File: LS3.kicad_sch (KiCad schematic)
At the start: 6 parts, among them Q5 VND14NV04-E, Q6 VND14NV04-E, Q7 VND14NV04-E

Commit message: Vendor DPAK/R0603 footprints for Update PCB without submodule gaps
Frame inj/LS sheets now use microcore-fp (in-repo footprints/) so KiCad
finds DPAK and R0603 even when hellen-one-common is missing from a zip
checkout. Keep hellen-one-common for Mini-B and other shared parts.
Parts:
- Q5, Q6, Q7: footprint hellen-one-common:DPAK -> microcore-fp:DPAK
- R5, R6, R7: footprint hellen-one-common:R0603 -> microcore-fp:R0603
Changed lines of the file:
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@@
 			)
 		)
-		(property "Footprint" "hellen-one-common:DPAK"
+		(property "Footprint" "microcore-fp:DPAK"
 			(at 101.6 25.4 0)
 			(effects
@@
 			)
 		)
-		(property "Footprint" "hellen-one-common:R0603"
+		(property "Footprint" "microcore-fp:R0603"
 			(at 139.7 25.4 0)
 			(effects
@@
 			)
 		)
-		(property "Footprint" "hellen-one-common:DPAK"
+		(property "Footprint" "microcore-fp:DPAK"
 			(at 101.6 55.879999999999995 0)
 			(effects
@@
 			)
 		)
-		(property "Footprint" "hellen-one-common:R0603"
+		(property "Footprint" "microcore-fp:R0603"
 			(at 139.7 55.879999999999995 0)
 			(effects
@@
 			)
 		)
-		(property "Footprint" "hellen-one-common:DPAK"
+		(property "Footprint" "microcore-fp:DPAK"
 			(at 101.6 86.36 0)
 			(effects
@@
 			)
 		)
-		(property "Footprint" "hellen-one-common:R0603"
+		(property "Footprint" "microcore-fp:R0603"
 			(at 139.7 86.36 0)
 			(effects

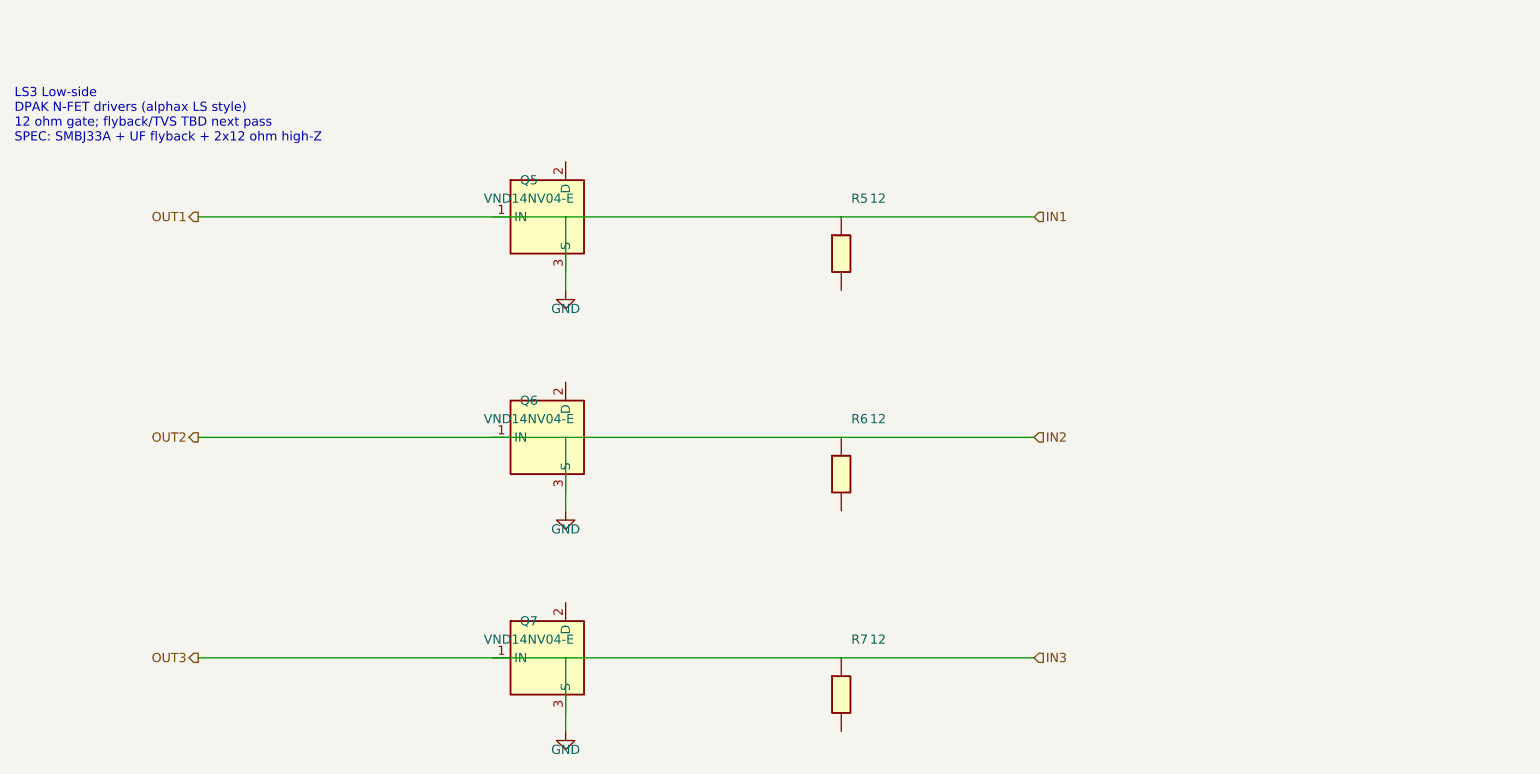
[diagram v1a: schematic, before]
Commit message: Fix top schematic wiring so labels connect to Hellen module pins
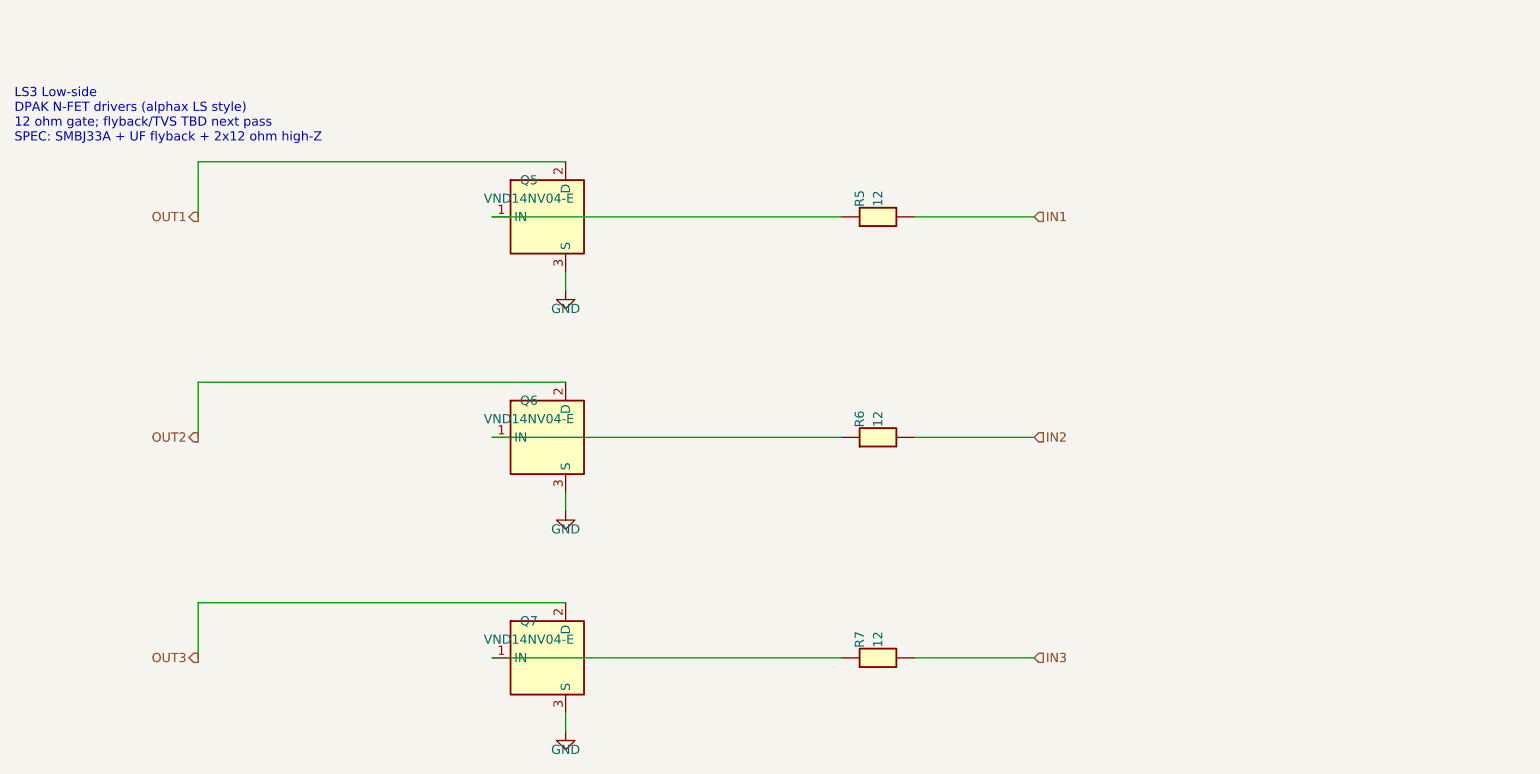
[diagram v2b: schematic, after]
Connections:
- net GND: now also Q5.3 (S), Q6.3 (S), Q7.3 (S); no longer R5.1, R6.1, R7.1
- net IN3: now reaches R7.2
- net at Q6.1 (IN): now also R6.1
- net OUT2: now reaches Q6.2 (D)
- net IN2: now reaches R6.2
- net at Q5.1 (IN): now also R5.1
- net OUT1: now reaches Q5.2 (D)
- net at Q7.1 (IN): now also R7.1
- net OUT3: now reaches Q7.2 (D)
- net IN1: now reaches R5.2
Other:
- moved on the sheet: R5, R6, R7
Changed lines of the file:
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@@
 	(symbol
 		(lib_id "hellen-one-common:Res")
-		(at 139.7 25.4 270)
+		(at 139.7 25.4 0)
 		(unit 1)
 		(exclude_from_sim no)
@@
 	(symbol
 		(lib_id "hellen-one-common:Res")
-		(at 139.7 55.879999999999995 270)
+		(at 139.7 55.879999999999995 0)
 		(unit 1)
 		(exclude_from_sim no)
@@
 	(symbol
 		(lib_id "hellen-one-common:Res")
-		(at 139.7 86.36 270)
+		(at 139.7 86.36 0)
 		(unit 1)
 		(exclude_from_sim no)
@@
 		)
 	)
-	(wire
-		(pts
-			(xy 50.8 25.4) (xy 101.6 25.4)
-		)
-		(stroke
-			(width 0)
-			(type default)
-		)
-	)
-	(wire
-		(pts
-			(xy 101.6 25.4) (xy 139.7 25.4)
-		)
-		(stroke
-			(width 0)
-			(type default)
-		)
-	)
-	(wire
-		(pts
-			(xy 139.7 25.4) (xy 166.37 25.4)
-		)
-		(stroke
-			(width 0)
-			(type default)
-		)
-	)
-	(wire
-		(pts
-			(xy 101.6 25.4) (xy 101.6 35.56)
-		)
-		(stroke
-			(width 0)
-			(type default)
-		)
-	)
-	(wire
-		(pts
-			(xy 50.8 55.879999999999995) (xy 101.6 55.879999999999995)
-		)
-		(stroke
-			(width 0)
-			(type default)
-		)
-	)
-	(wire
-		(pts
-			(xy 101.6 55.879999999999995) (xy 139.7 55.879999999999995)
-		)
-		(stroke
-			(width 0)
-			(type default)
-		)
-	)
-	(wire
-		(pts
-			(xy 139.7 55.879999999999995) (xy 166.37 55.879999999999995)
-		)
-		(stroke
-			(width 0)
-			(type default)
-		)
-	)
-	(wire
-		(pts
-			(xy 101.6 55.879999999999995) (xy 101.6 66.03999999999999)
-		)
-		(stroke
-			(width 0)
-			(type default)
-		)
-	)
-	(wire
-		(pts
-			(xy 50.8 86.36) (xy 101.6 86.36)
-		)
-		(stroke
-			(width 0)
-			(type default)
-		)
-	)
-	(wire
-		(pts
-			(xy 101.6 86.36) (xy 139.7 86.36)
-		)
-		(stroke
-			(width 0)
-			(type default)
-		)
-	)
-	(wire
-		(pts
-			(xy 139.7 86.36) (xy 166.37 86.36)
-		)
-		(stroke
-			(width 0)
-			(type default)
-		)
-	)
-	(wire
-		(pts
-			(xy 101.6 86.36) (xy 101.6 96.52)
-		)
-		(stroke
-			(width 0)
-			(type default)
-		)
-	)
 	(text "LS3 Low-side\nDPAK N-FET drivers (alphax LS style)\n12 ohm gate; flyback/TVS TBD next pass\nSPEC: SMBJ33A + UF flyback + 2x12 ohm high-Z"
 		(at 25.4 15.24 0)
@@
 		)
 	)
+	(wire
+		(pts
+			(xy 50.8 25.4) (xy 50.8 17.78)
+		)
+		(stroke
+			(width 0)
+			(type default)
+		)
+	)
+	(wire
+		(pts
+			(xy 50.8 17.78) (xy 101.6 17.78)
+		)
+		(stroke
+			(width 0)
+			(type default)
+		)
+	)
+	(wire
+		(pts
+			(xy 101.6 33.02) (xy 101.6 35.56)
+		)
+		(stroke
+			(width 0)
+			(type default)
+		)
+	)
+	(wire
+		(pts
+			(xy 166.37 25.4) (xy 149.86 25.4)
+		)
+		(stroke
+			(width 0)
+			(type default)
+		)
+	)
+	(wire
+		(pts
+			(xy 139.7 25.4) (xy 91.44 25.4)
+		)
+		(stroke
+			(width 0)
+			(type default)
+		)
+	)
+	(wire
+		(pts
+			(xy 50.8 55.88) (xy 50.8 48.26)
+		)
+		(stroke
+			(width 0)
+			(type default)
+		)
+	)
+	(wire
+		(pts
+			(xy 50.8 48.26) (xy 101.6 48.26)
+		)
+		(stroke
+			(width 0)
+			(type default)
+		)
+	)
+	(wire
+		(pts
+			(xy 101.6 63.5) (xy 101.6 66.04)
+		)
+		(stroke
+			(width 0)
+			(type default)
+		)
+	)
+	(wire
+		(pts
+			(xy 166.37 55.88) (xy 149.86 55.88)
+		)
+		(stroke
+			(width 0)
+			(type default)
+		)
+	)
+	(wire
+		(pts
+			(xy 139.7 55.88) (xy 91.44 55.88)
+		)
+		(stroke
+			(width 0)
+			(type default)
+		)
+	)
+	(wire
+		(pts
+			(xy 50.8 86.36) (xy 50.8 78.74)
+		)
+		(stroke
+			(width 0)
+			(type default)
+		)
+	)
+	(wire
+		(pts
+			(xy 50.8 78.74) (xy 101.6 78.74)
+		)
+		(stroke
+			(width 0)
+			(type default)
+		)
+	)
+	(wire
+		(pts
+			(xy 101.6 93.98) (xy 101.6 96.52)
+		)
+		(stroke
+			(width 0)
+			(type default)
+		)
+	)
+	(wire
+		(pts
+			(xy 166.37 86.36) (xy 149.86 86.36)
+		)
+		(stroke
+			(width 0)
+			(type default)
+		)
+	)
+	(wire
+		(pts
+			(xy 139.7 86.36) (xy 91.44 86.36)
+		)
+		(stroke
+			(width 0)
+			(type default)
+		)
+	)

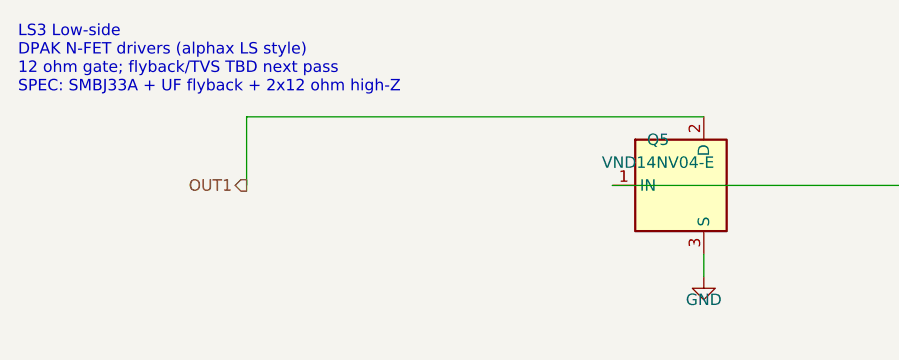
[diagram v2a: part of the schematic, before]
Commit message: Rev j: injector SMAJ33A TVS, US1M flyback, and 2nd 12Ω per INJ channel
SPEC power-stage protection on INJ4 sch+PCB: R8–R11 ballast, D1–D4 US1M,
D5–D8 SMAJ33A (DO-214AC equivalent of SMBJ33A). FET cluster left in place;
new parts in alley + pocket C. BOARD_REVISION bumped to j. PCB remains
substantial (zones + aux origin intact).

Co-authored-by: Quintin <quintinbannink42@users.noreply.github.com>
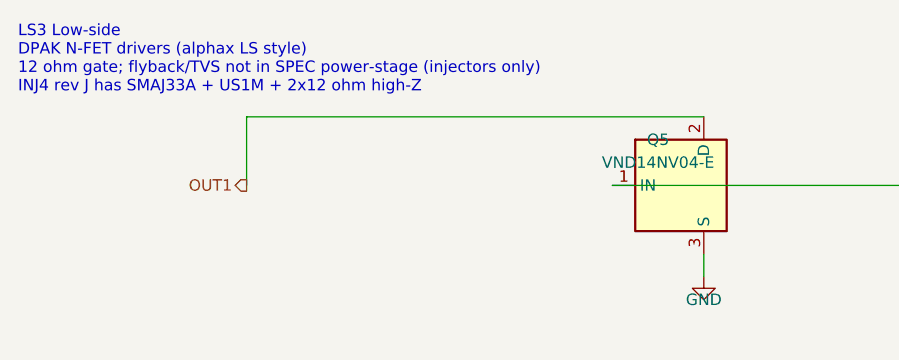
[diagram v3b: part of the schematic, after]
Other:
- note added: "LS3 Low-side DPAK N-FET drivers (alphax LS style) 12 ohm gate; flyback/TVS not in SPEC power-stage (injectors only) INJ4 rev J has SMAJ33A + US1M + 2x12 ohm high-Z"
- note removed: "LS3 Low-side DPAK N-FET drivers (alphax LS style) 12 ohm gate; flyback/TVS TBD next pass SPEC: SMBJ33A + UF flyback + 2x12 ohm high-Z"
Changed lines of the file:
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@@
 		)
 	)
-	(text "LS3 Low-side\nDPAK N-FET drivers (alphax LS style)\n12 ohm gate; flyback/TVS TBD next pass\nSPEC: SMBJ33A + UF flyback + 2x12 ohm high-Z"
+	(text "LS3 Low-side\nDPAK N-FET drivers (alphax LS style)\n12 ohm gate; flyback/TVS not in SPEC power-stage (injectors only)\nINJ4 rev J has SMAJ33A + US1M + 2x12 ohm high-Z"
 		(at 25.4 15.24 0)
 		(effects

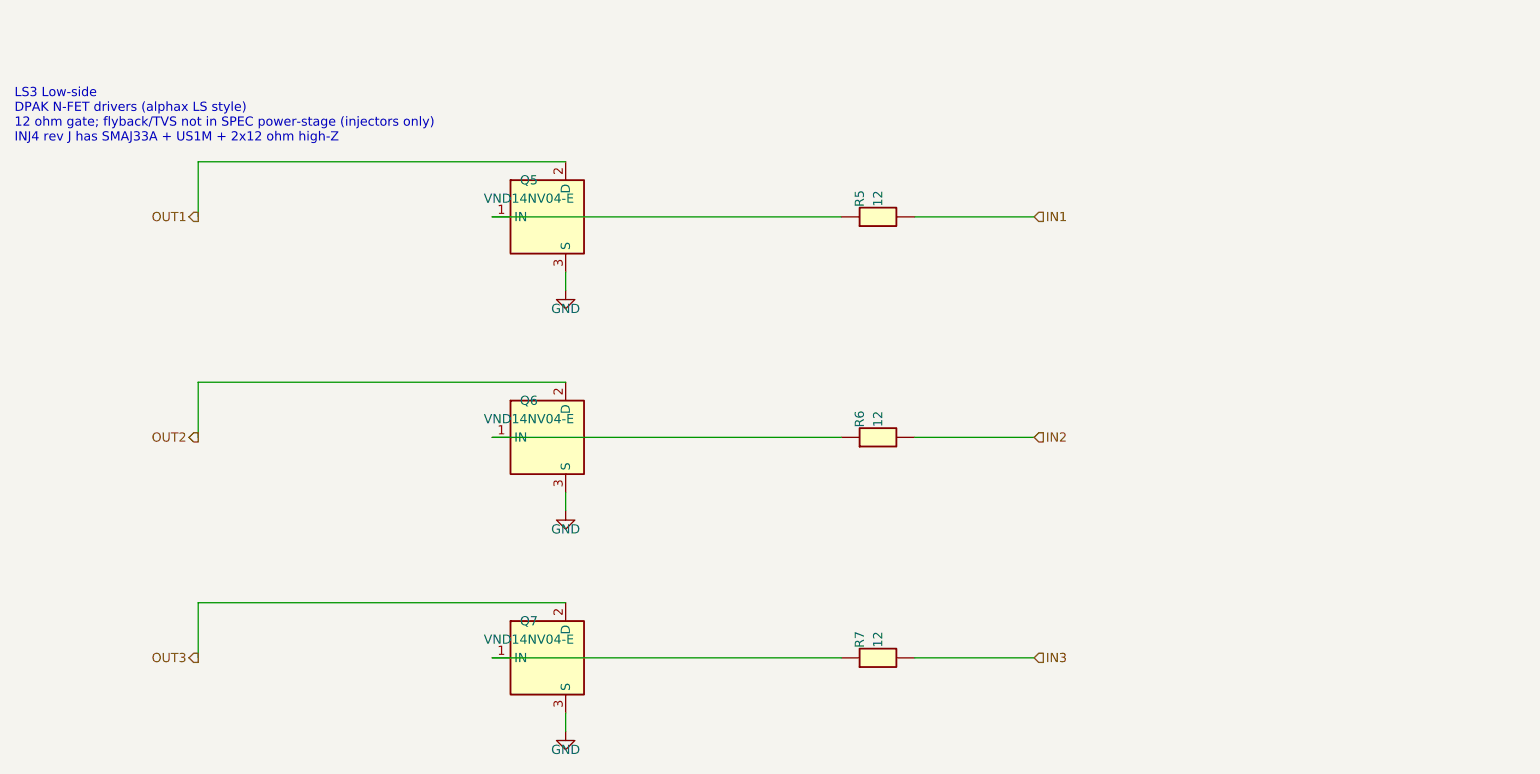
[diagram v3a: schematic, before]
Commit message: Rev n: F407 on mega-mcu100 and drop LS FETs
Swap module U105 from STM32F429VIT6 (C92002) to STM32F407VGT6
(LCSC C12345) in bom_replace_microcore-n.csv. Keep mega-mcu100/0.3.

Remove Q5-Q7 and gate R5-R7 from the LS3 sheet and the PCB, including
their tracks and vias. AMPSEAL pins 8/9/10 are reserved / NC.

Co-authored-by: Quintin <quintinbannink42@users.noreply.github.com>
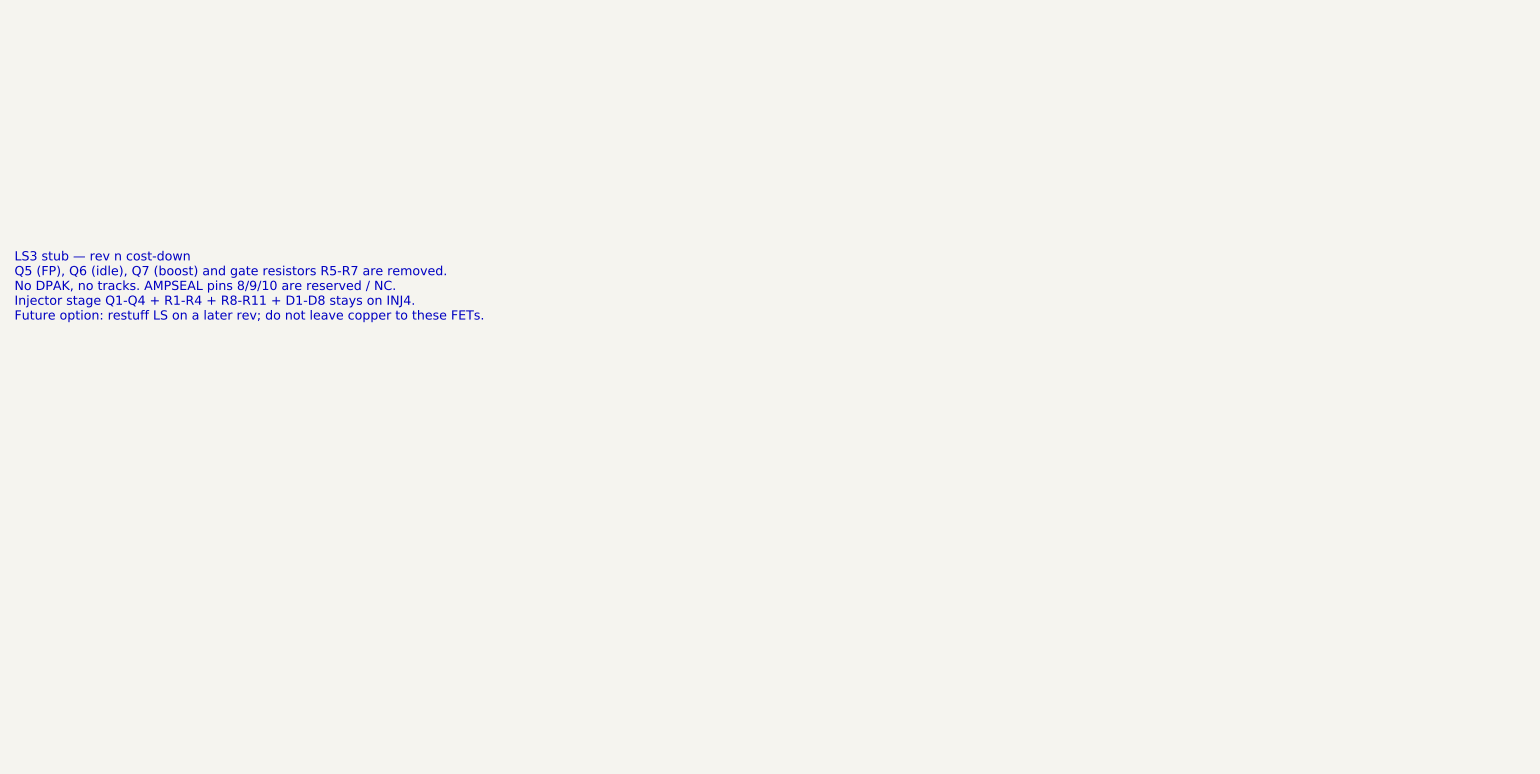
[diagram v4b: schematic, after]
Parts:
- removed Q5, Q6, Q7: VND14NV04-E, microcore-fp:DPAK, symbol Power_Management:AUIPS2041L
- removed R5, R6, R7: 12, microcore-fp:R0603, symbol hellen-one-common:Res
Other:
- note added: "LS3 stub — rev n cost-down Q5 (FP), Q6 (idle), Q7 (boost) and gate resistors R5-R7 are removed. No DPAK, no tracks. AMPSEAL pins 8/9/10 are reserved / NC. Injector stage Q1-Q4 + R1-R4 + R8-R11 + D1-D8 stays on INJ4. Future option: restuff LS on a later rev; do not leave copper to these FETs."
- note removed: "LS3 Low-side DPAK N-FET drivers (alphax LS style) 12 ohm gate; flyback/TVS not in SPEC power-stage (injectors only) INJ4 rev J has SMAJ33A + US1M + 2x12 ohm high-Z"

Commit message: Rev o: NCE4080K on Q1-Q7 and restore LS FETs
Swap every power FET from VND14NV04-E to NCE4080K (LCSC C191380,
TO-252-2L) on the existing DPAK land. Bring back Q5-Q7 and gate
R5-R7, and put AMPSEAL pins 8/9/10 back to fuel pump, idle, and boost.

F407VGT6 on mega-mcu100, injector TVS/flyback, Core EFI silk, GND
pours, and the drill origin stay. RDS(on) is rated at 10 V; the
3.3 V gate has no added driver.

Co-authored-by: Quintin <quintinbannink42@users.noreply.github.com>
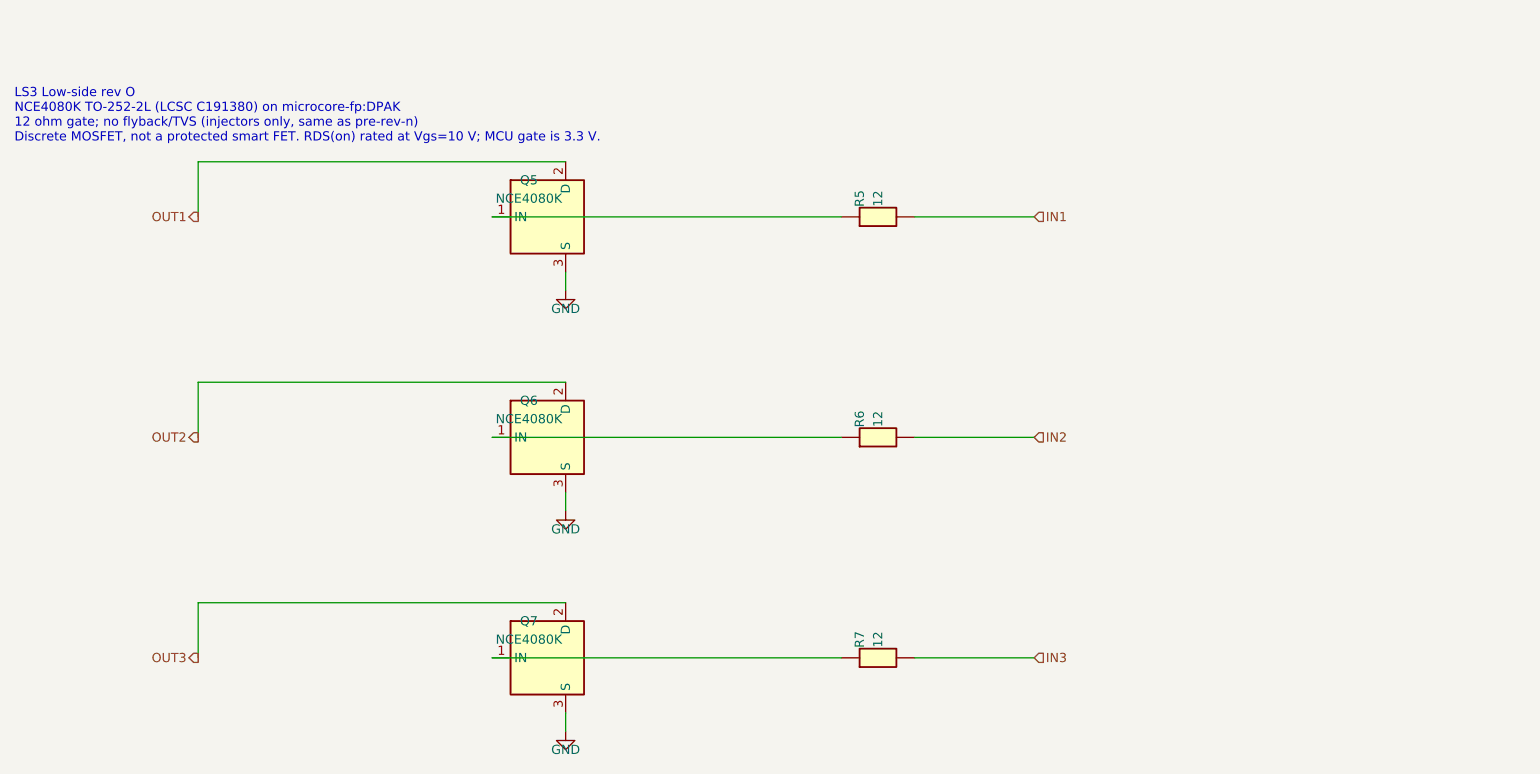
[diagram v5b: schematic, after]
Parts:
- added Q5, Q6, Q7: NCE4080K, microcore-fp:DPAK, symbol Power_Management:AUIPS2041L
- added R5, R6, R7: 12, microcore-fp:R0603, symbol hellen-one-common:Res
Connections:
- new net: Q7.1 (IN), R7.1
- new net: Q6.1 (IN), R6.1
- new net: Q5.1 (IN), R5.1
- new net GND: Q5.3 (S), Q6.3 (S), Q7.3 (S)
- new net IN1: R5.2
- new net IN2: R6.2
- new net IN3: R7.2
- new net OUT1: Q5.2 (D)
- new net OUT2: Q6.2 (D)
- new net OUT3: Q7.2 (D)
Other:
- note added: "LS3 Low-side rev O NCE4080K TO-252-2L (LCSC C191380) on microcore-fp:DPAK 12 ohm gate; no flyback/TVS (injectors only, same as pre-rev-n) Discrete MOSFET, not a protected smart FET. RDS(on) rated at Vgs=10 V; MCU gate is 3.3 V."
- note removed: "LS3 stub — rev n cost-down Q5 (FP), Q6 (idle), Q7 (boost) and gate resistors R5-R7 are removed. No DPAK, no tracks. AMPSEAL pins 8/9/10 are reserved / NC. Injector stage Q1-Q4 + R1-R4 + R8-R11 + D1-D8 stays on INJ4. Future option: restuff LS on a later rev; do not leave copper to these FETs."
